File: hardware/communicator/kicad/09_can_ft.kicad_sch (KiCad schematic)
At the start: 12 parts, among them U22 MAX3055ASD+, U23 SN74LVC2G17DCKR

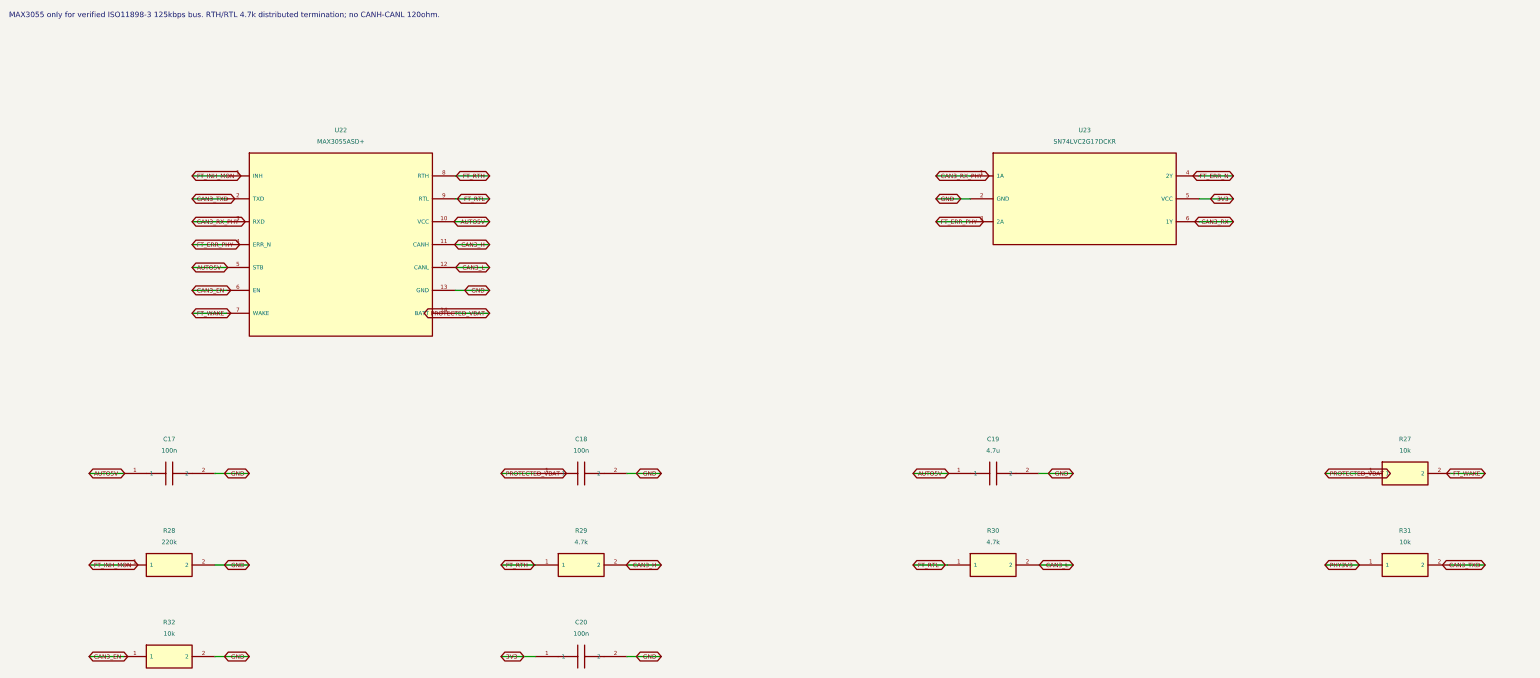
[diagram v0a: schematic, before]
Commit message: feat: add R1 detailed hardware and navigation protocol review candidate
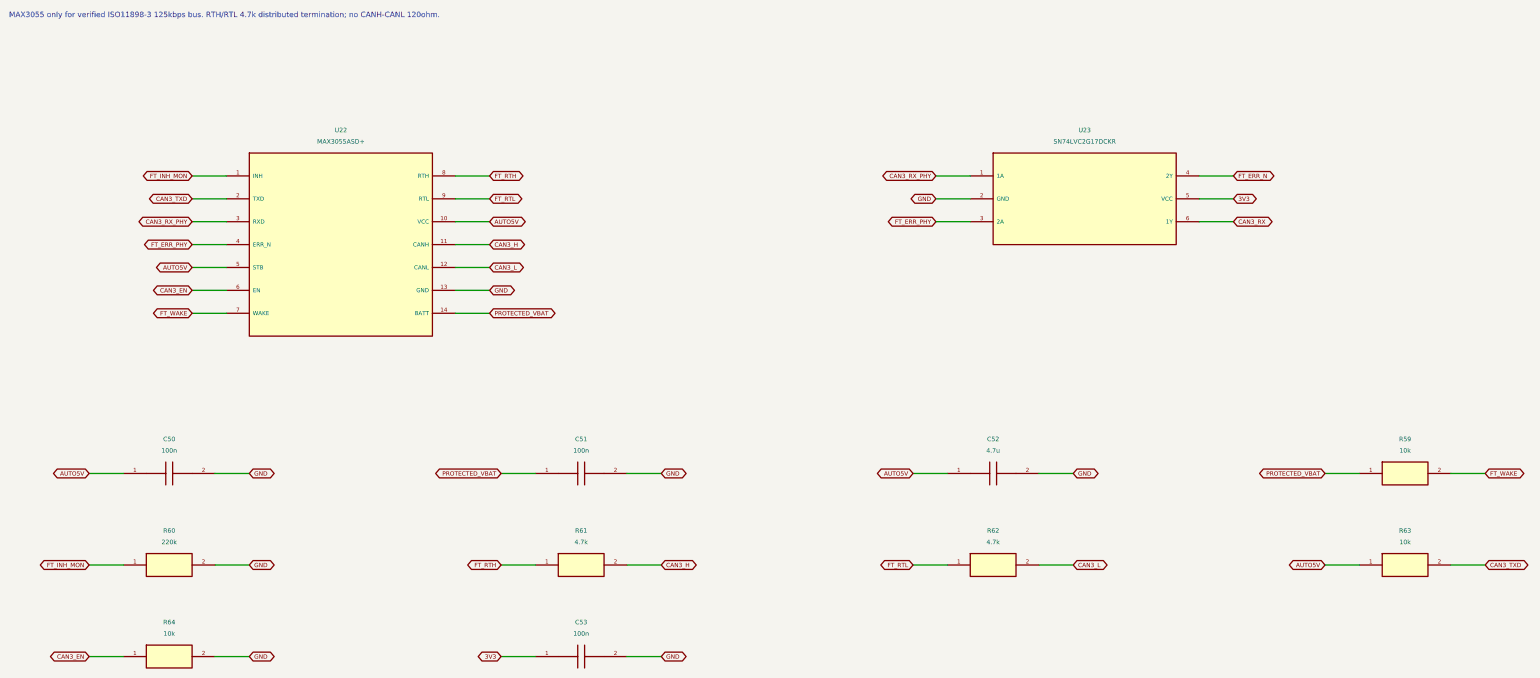
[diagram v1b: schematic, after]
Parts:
- removed C17: 100n, CANView:Capacitor_SMD__C_0402_1005Metric, symbol CANView:CANView_communicator_C17
- removed C18: 100n, CANView:Capacitor_SMD__C_0603_1608Metric, symbol CANView:CANView_communicator_C18
- removed C19: 4.7u, CANView:Capacitor_SMD__C_0603_1608Metric, symbol CANView:CANView_communicator_C19
- removed C20: 100n, CANView:Capacitor_SMD__C_0402_1005Metric, symbol CANView:CANView_communicator_C20
- removed R27: 10k, CANView:Resistor_SMD__R_0603_1608Metric, symbol CANView:CANView_communicator_R27
- removed R28: 220k, CANView:Resistor_SMD__R_0603_1608Metric, symbol CANView:CANView_communicator_R28
- removed R29: 4.7k, CANView:Resistor_SMD__R_0805_2012Metric, symbol CANView:CANView_communicator_R29
- removed R30: 4.7k, CANView:Resistor_SMD__R_0805_2012Metric, symbol CANView:CANView_communicator_R30
- removed R31: 10k, CANView:Resistor_SMD__R_0402_1005Metric, symbol CANView:CANView_communicator_R31
- removed R32: 10k, CANView:Resistor_SMD__R_0402_1005Metric, symbol CANView:CANView_communicator_R32
- added C50: 100n, CANView:Capacitor_SMD__C_0402_1005Metric, symbol CANView:CANView_communicator_C50
- added C51: 100n, CANView:Capacitor_SMD__C_0603_1608Metric, symbol CANView:CANView_communicator_C51
- added C52: 4.7u, CANView:Capacitor_SMD__C_0603_1608Metric, symbol CANView:CANView_communicator_C52
- added C53: 100n, CANView:Capacitor_SMD__C_0402_1005Metric, symbol CANView:CANView_communicator_C53
- added R59: 10k, CANView:Resistor_SMD__R_0603_1608Metric, symbol CANView:CANView_communicator_R59
- added R60: 220k, CANView:Resistor_SMD__R_0603_1608Metric, symbol CANView:CANView_communicator_R60
- added R61: 4.7k, CANView:Resistor_SMD__R_0805_2012Metric, symbol CANView:CANView_communicator_R61
- added R62: 4.7k, CANView:Resistor_SMD__R_0805_2012Metric, symbol CANView:CANView_communicator_R62
- added R63: 10k, CANView:Resistor_SMD__R_0402_1005Metric, symbol CANView:CANView_communicator_R63
- added R64: 10k, CANView:Resistor_SMD__R_0402_1005Metric, symbol CANView:CANView_communicator_R64
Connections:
- net 3V3: now also C53.1
- net AUTO5V: now also C50.1, C52.1, R63.1
- net CAN3_EN: now also R64.1
- net CAN3_H: now also R61.2
- net CAN3_L: now also R62.2
- net CAN3_TXD: now also R63.2
- net FT_INH_MON: now also R60.1
- net FT_RTH: now also R61.1
- net FT_RTL: now also R62.1
- net FT_WAKE: now also R59.2
- net GND: now also C50.2, C51.2, C52.2, C53.2, R60.2, R64.2
- net PROTECTED_VBAT: now also C51.1, R59.1

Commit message: fix: close hardware rail-fault paths and sensor contract gaps
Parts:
- removed C50: 100n, CANView:Capacitor_SMD__C_0402_1005Metric, symbol CANView:CANView_communicator_C50
- removed C51: 100n, CANView:Capacitor_SMD__C_0603_1608Metric, symbol CANView:CANView_communicator_C51
- removed R59: 10k, CANView:Resistor_SMD__R_0603_1608Metric, symbol CANView:CANView_communicator_R59
- added C54: 4.7u, CANView:Capacitor_SMD__C_0603_1608Metric, symbol CANView:CANView_communicator_C54
- added C55: 100n, CANView:Capacitor_SMD__C_0402_1005Metric, symbol CANView:CANView_communicator_C55
- added R65: 10k, CANView:Resistor_SMD__R_0402_1005Metric, symbol CANView:CANView_communicator_R65
- C52: value 4.7u -> 100n; footprint CANView:Capacitor_SMD__C_0603_1608Metric -> CANView:Capacitor_SMD__C_0402_1005Metric; MPN GEN-C-0603-4.7u-16V-X7R -> GEN-C-0402-100n-16V-X7R
- C53: footprint CANView:Capacitor_SMD__C_0402_1005Metric -> CANView:Capacitor_SMD__C_0603_1608Metric; MPN GEN-C-0402-100n-16V-X7R -> GEN-C-0603-100n-50V-X7R; Specification 16V; ±10%; X7R; -55..125C; verify effective capacitance und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 -> 50V; ±10%; X7R; -55..125C; verify effective capacitance und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
- R60: value 220k -> 10k; MPN GEN-R-0603-220k-1% -> GEN-R-0603-10k-1%
- R61: value 4.7k -> 220k; footprint CANView:Resistor_SMD__R_0805_2012Metric -> CANView:Resistor_SMD__R_0603_1608Metric; MPN GEN-R-0805-4.7k-1% -> GEN-R-0603-220k-1%; Specification 0.25W; 100V; ±1%; ±100ppm/K; -55..155C -> 0.1W; 50V; ±1%; ±100ppm/K; -55..155C
- R63: value 10k -> 4.7k; footprint CANView:Resistor_SMD__R_0402_1005Metric -> CANView:Resistor_SMD__R_0805_2012Metric; MPN GEN-R-0402-10k-1% -> GEN-R-0805-4.7k-1%; Specification 0.1W; 50V; ±1%; ±100ppm/K; -55..155C -> 0.25W; 100V; ±1%; ±100ppm/K; -55..155C
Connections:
- net 3V3: now also C55.1; no longer C53.1
- net AUTO5V: now also R64.1, C54.1; no longer R63.1
- net CAN3_EN: now also R65.1; no longer R64.1
- net CAN3_H: now also R62.2; no longer R61.2
- net CAN3_L: now also R63.2; no longer R62.2
- net CAN3_TXD: now also R64.2; no longer R63.2
- net FT_INH_MON: now also R61.1; no longer R60.1
- net FT_RTH: now also R62.1; no longer R61.1
- net FT_RTL: now also R63.1; no longer R62.1
- net FT_WAKE: now also R60.2
- net GND: now also R61.2, C54.2, C55.2, R65.2; no longer R60.2, R64.2
- net PROTECTED_VBAT: now also C53.1, R60.1
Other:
- moved on the sheet: C52, C53, R60, R61, R62, R63, R64
